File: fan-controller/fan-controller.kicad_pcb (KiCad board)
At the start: 2 copper layers, 80 x 60 mm, 23 parts, among them J1 DC_Jack_12V, J2 FAN1, J3 FAN2, J4 FAN3, J5 FAN4, U1 XIAO ESP32-C3, U2 AMS1117-5.0

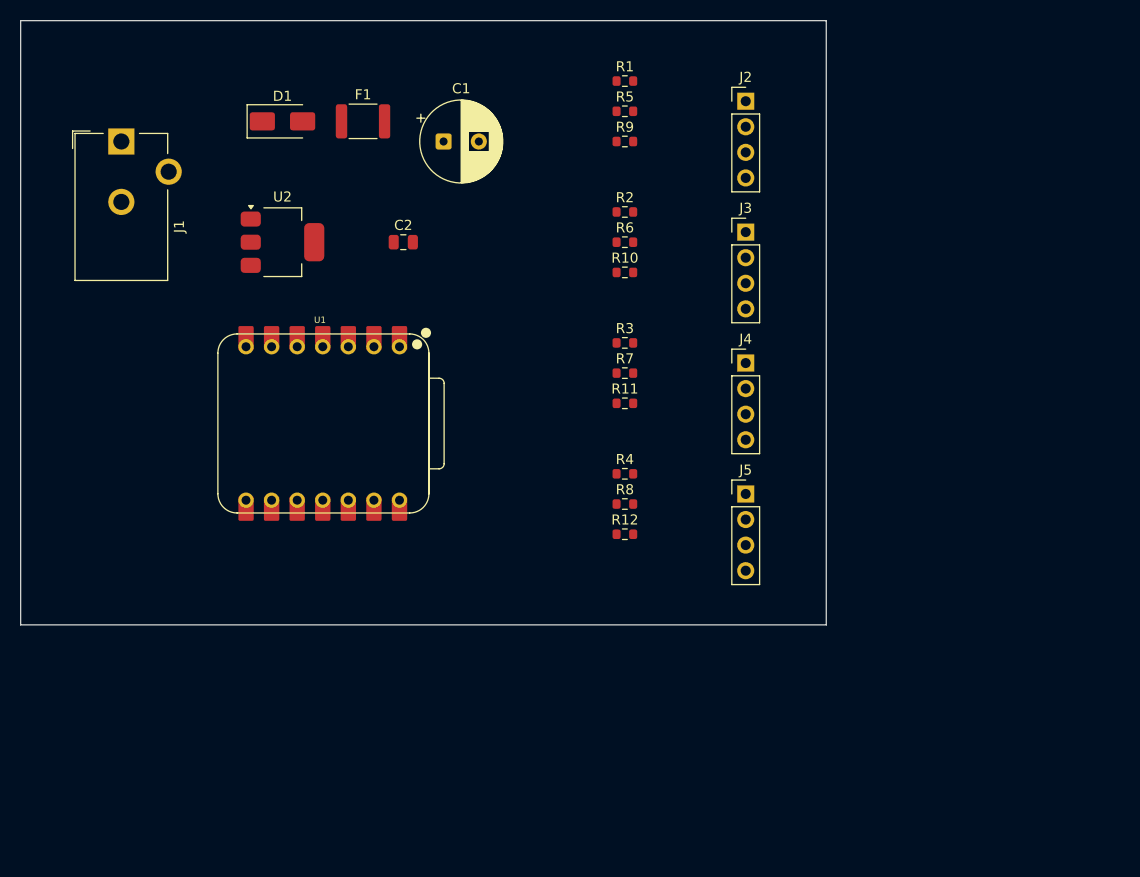
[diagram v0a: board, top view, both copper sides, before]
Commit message: Fold every schematic step into generate.py; swap fan pin pairs
generate.py is now the only command needed to rebuild the schematic. It runs
the full sequence, because each step used to be separate and every one of them
was forgotten at least once:

  1. reposition symbols and redraw all nets   (validated before writing)
  2. repair structural defects                (was fix_sch.py, now deleted)
  3. re-attach PWR_FLAGs and no-connects      (was an ad-hoc snippet, retyped
                                               by hand three times)
  4. verify the netlist against netplan.py    (was a separate audit)

Step 4 matters most: ERC cannot catch a wire landing on the wrong real pin,
since that is still a legal connection. Only a pin-by-pin netlist diff does.
--no-verify skips it where kicad-cli is unavailable.

Two latent bugs fixed while integrating:

  * Placed symbols were matched with a single-line regex, but KiCad rewrites
    the file with each field on its own line whenever the schematic is opened
    in the GUI. Regenerating after any GUI session found zero symbols and
    failed; fix_sch.py hit the same thing but failed silently, reporting
    success while repairing nothing. Both paths now use a whitespace-tolerant
    SYMBOL_RE, and a symbol's (at ...) is rewritten by matched span rather
    than by reconstructing the literal text.

  * netplan.py had lost pin_abs_rot, which only ever existed in a session
    scratchpad that a crash wiped. Restored and re-verified empirically
    against all four rotations before use.

Also swaps the XIAO pins between FAN1/FAN2 and FAN3/FAN4 as requested:
  FAN1 D1/D2 (2,3)   FAN2 D3/D4 (4,5)
  FAN3 D7/D10 (8,11) FAN4 D5/D6 (6,7)

PCB synced: 16 U1 pad assignments updated (8 pins x 2, since the DIP
footprint pairs an SMD and a through-hole pad per number). All 22 nets
cross-checked between schematic and board.

Board also reworked earlier in this session: outline fitted to the ground
zone at 76.5 x 29 mm (was 80 x 60), J1 m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
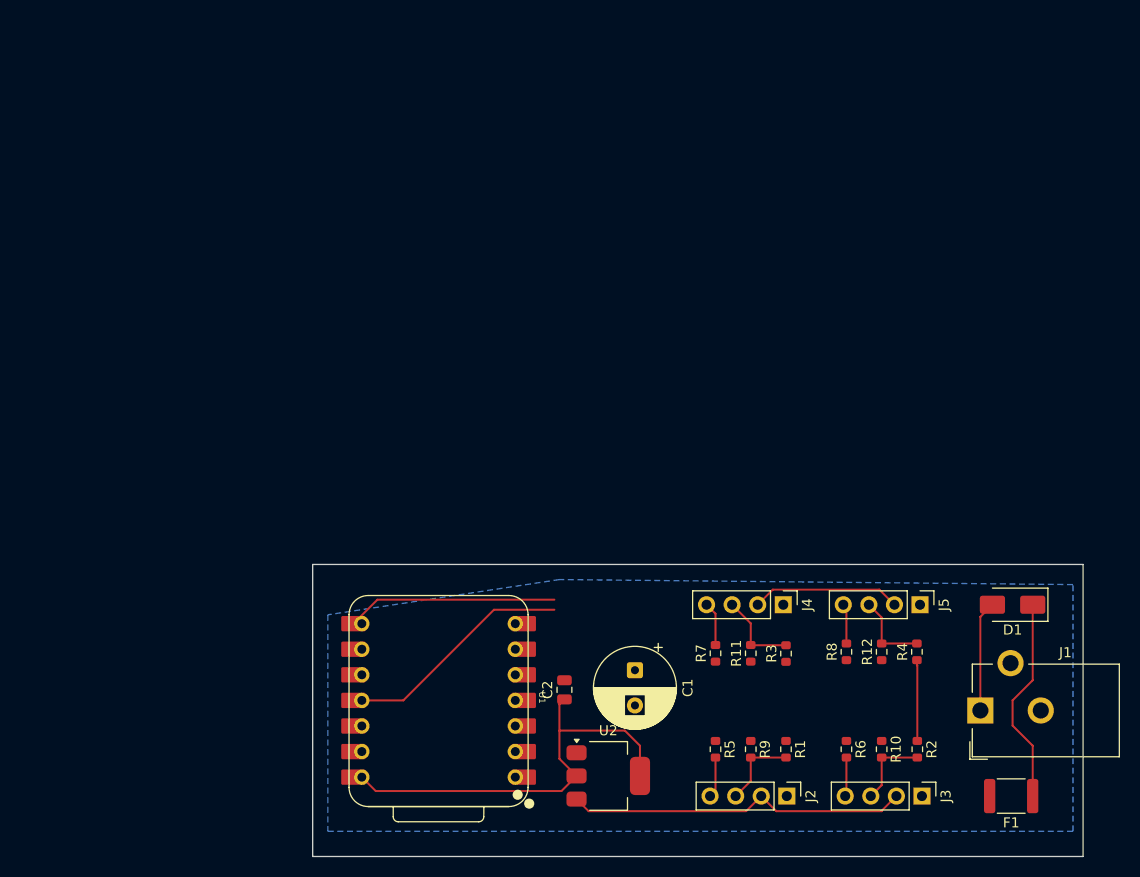
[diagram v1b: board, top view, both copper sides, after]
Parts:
- C1: footprint CP_Radial_D8.0mm_P3.50mm -> Capacitor_THT:CP_Radial_D8.0mm_P3.50mm
- C2: footprint C_0805_2012Metric -> Capacitor_SMD:C_0805_2012Metric
- D1: footprint D_SMA -> Diode_SMD:D_SMA
- F1: footprint Fuse_1812_4532Metric -> Fuse:Fuse_1812_4532Metric
- J1: footprint BarrelJack_CUI_PJ-102AH_Horizontal -> Connector_BarrelJack:BarrelJack_CUI_PJ-102AH_Horizontal
- J2, J3, J4, J5: footprint PinHeader_1x04_P2.54mm_Vertical -> Connector_PinHeader_2.54mm:PinHeader_1x04_P2.54mm_Vertical
- R1, R10, R11, R12, R2, R3, R4, R5, R6, R7, R8, R9: footprint R_0603_1608Metric -> Resistor_SMD:R_0603_1608Metric
- U1: footprint XIAO-ESP32-C3-DIP -> Seeed_Studio_XIAO_Series:XIAO-ESP32-C3-DIP
- U2: footprint SOT-223-3_TabPin2 -> Package_TO_SOT_SMD:SOT-223-3_TabPin2
- moved J1 102.3 mm to (95.3, 68.5), turned to 90 degrees
- moved F1 92.9 mm to (98.4, 77.0), turned to 180 degrees
- moved D1 86.9 mm to (98.5, 58.0), turned to 180 degrees
- moved J2 69.1 mm to (76.1, 77.0), turned to -90 degrees
- moved R1 68.3 mm to (76.0, 72.3), turned to -90 degrees
- moved R5 64.0 mm to (69.0, 72.3), turned to -90 degrees
- moved U2 62.1 mm to (58.4, 75.0)
- moved R9 61.6 mm to (72.5, 72.3), turned to -90 degrees
- moved R2 60.7 mm to (89.0, 72.3), turned to -90 degrees
- moved J3 58.7 mm to (89.5, 77.0), turned to -90 degrees
- moved C1 55.8 mm to (61.0, 64.5), turned to -90 degrees
- moved R6 54.9 mm to (82.0, 72.3), turned to -90 degrees
- moved R10 53.8 mm to (85.5, 72.3), turned to -90 degrees
- moved C2 47.2 mm to (54.0, 66.5), turned to 90 degrees
- moved R3 34.8 mm to (76.0, 62.9), turned to 90 degrees
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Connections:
- U1 pad 11: /FAN4_TACH -> /FAN3_TACH
- U1 pad 6: /FAN3_PWM -> /FAN4_PWM
- U1 pad 7: /FAN3_TACH -> /FAN4_TACH
- U1 pad 8: /FAN4_PWM -> /FAN3_PWM
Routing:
- net /+12V_PROT: track 0.00 -> 49.0 mm
- net /+5V: track 0.00 -> 42.6 mm
- net /FAN3_TACH: track 0.00 -> 22.8 mm
- net /FAN3_PWM: track 0.00 -> 20.9 mm
- net /+12V_FUSED: track 0.00 -> 20.7 mm
- net /+12V_IN: track 0.00 -> 11.0 mm
- net /FAN3_TACH_RAW: track 0.00 -> 8.28 mm
- net /+3V3: track 0.00 -> 8.04 mm
- net /FAN1_TACH_RAW: track 0.00 -> 7.95 mm
- net /FAN4_TACH_RAW: track 0.00 -> 7.88 mm
- net /FAN2_TACH_RAW: track 0.00 -> 7.81 mm
- net /FAN3_PWM_OUT: track 0.00 -> 4.37 mm
- net /FAN1_PWM_OUT: track 0.00 -> 4.05 mm
- net /FAN4_PWM_OUT: track 0.00 -> 3.98 mm
- net /FAN2_PWM_OUT: track 0.00 -> 3.87 mm
- added copper zone on B.Cu, net /GND
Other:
- board size 80 x 60 mm -> 76.5 x 29 mm

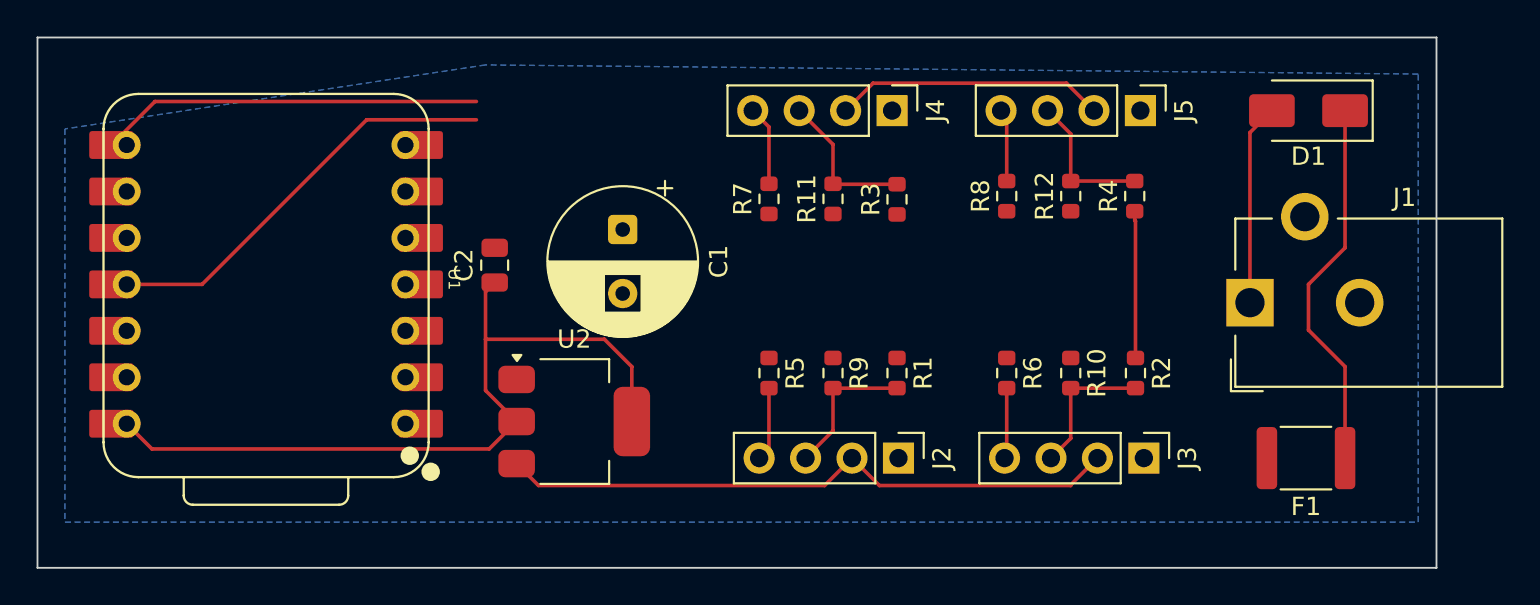
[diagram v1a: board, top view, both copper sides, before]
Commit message: Route the board: ground plane, wider power nets, jack on the edge
The PCB is now fully routed. 167 tracks, 7 vias, no unconnected pads.

Layout
  Board shrunk from 80 x 60 mm to 72.9 x 25.0 mm, fitted 1mm clear of all
  copper. J1 sits on the right end opposite the XIAO with its flange on the
  board edge, so the 3.5mm barrel protrudes as a panel-mount jack should.
  Getting there took two goes: the flange initially sat 1.9mm inboard of the
  edge, making the plug look adrift. Moving the plug pocket (J1, F1, D1 plus
  9 tracks) 1.8mm inward fixed it. 3mm was requested but drives F1's pad and
  the +12V_IN wire into the +12V_PROT trunk at x=91.5; 1.8mm is the limit
  before that clash. Only the 2 tracks crossing the pocket boundary needed
  shortening, exactly as predicted.

Ground plane
  GND pour on B.Cu, 1417mm^2, thermal relief on pads. A keep-out clears the
  copper away from the XIAO's antenna: U1 is rotated -90 so pins 7 and 8 both
  sit at y=59.88, the module's top edge, which is the antenna end opposite
  the USB connector. The window stops at y=58.6, clearing those two pads by
  0.52mm - an earlier attempt ran to y=60.0 and DRC rightly rejected it for
  swallowing them.

Track widths
  Power and ground widened from the 0.2mm minimum (0.74A) to targets from
  IPC-2152 at 1oz, 10C rise. A single width does not fit: the corridor around
  U1 is a 2.54mm pad pitch. So each segment starts at target and steps down
  only where DRC objects.

    +12V_IN, +12V_FUSED, +12V_PROT   1.0mm    2.39 A
    GND                              1.0mm    2.39 A  (2 segments 0.2mm)
    +5V, +3V3                        0.6mm    1.65 A

  The 12V rail feeds four fans through a 1.5A-hold polyfuse, so 2.39A leaves
  real margin. The two 0.2mm GND segments run directly over the B.Cu plane -
  sampling along their length found plane copper at 28 of 33 points, and U1's
  GND pad is a through-hole tied into it - so the plane carries that return
  in parallel and width is not the limit ther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
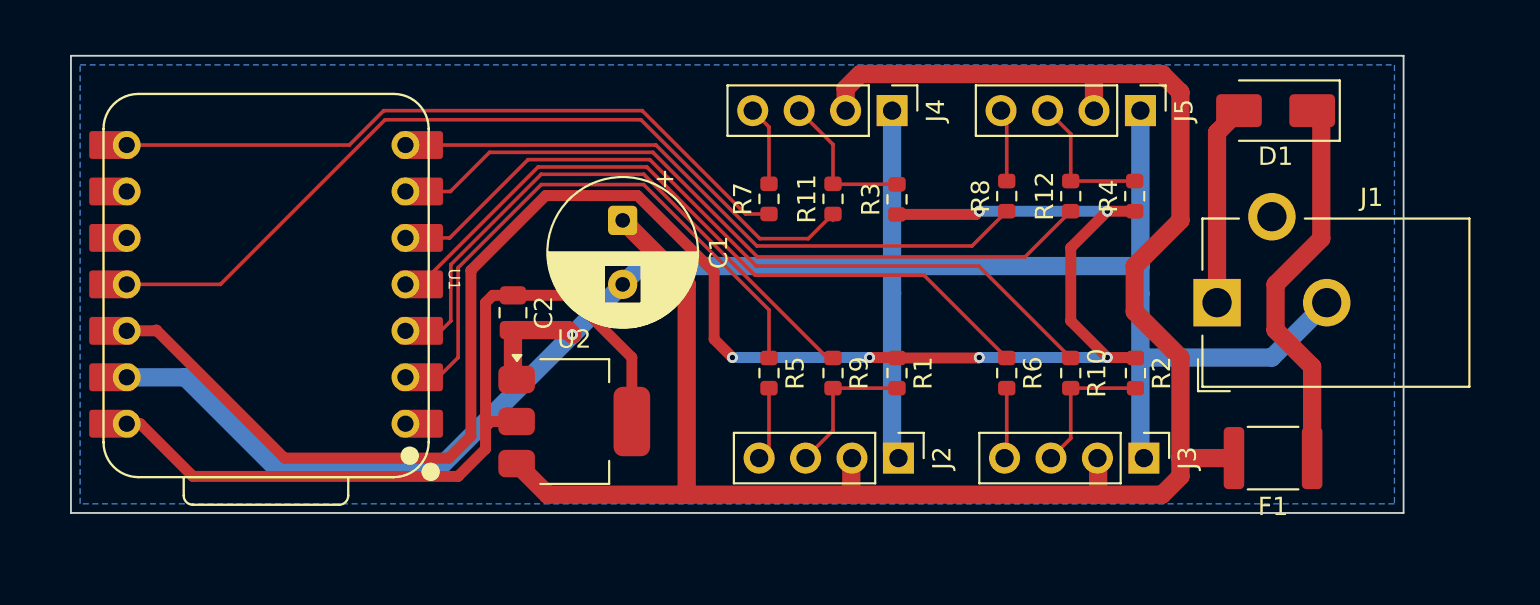
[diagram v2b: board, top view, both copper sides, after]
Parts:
- moved C2 2.79 mm to (55.0, 69.0), turned to -90 degrees
- moved D1 1.80 mm to (96.7, 58.0)
- moved F1 1.80 mm to (96.6, 77.0)
- moved J1 1.80 mm to (93.5, 68.5)
- moved C1 0.50 mm to (61.0, 64.0)
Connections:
- U1 pad 6: /FAN4_PWM -> /FAN4_TACH
- U1 pad 7: /FAN4_TACH -> /FAN4_PWM
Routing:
- net /GND: track 0.00 -> 117.8 mm, vias 0 -> 1
- net /+3V3: track 8.04 -> 97.9 mm, vias 0 -> 6
- net /+12V_PROT: track 49.0 -> 106.2 mm
- net /FAN2_TACH: track 0.00 -> 41.8 mm
- net /FAN2_PWM: track 0.00 -> 40.3 mm
- net /FAN4_TACH: track 0.00 -> 39.8 mm
- net /FAN4_PWM: track 0.00 -> 35.1 mm
- net /FAN1_TACH: track 0.00 -> 32.1 mm
- net /FAN1_PWM: track 0.00 -> 31.9 mm
- net /FAN3_TACH: track 22.8 -> 45.9 mm
- net /FAN3_PWM: track 20.9 -> 38.2 mm
- net /+5V: track 42.6 -> 44.2 mm
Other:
- board size 76.5 x 29 mm -> 72.9 x 25 mm

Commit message: Add back-side silkscreen: project name, author, year
Zwei Zeilen auf B.SilkS, mittig zwischen den Steckern bei (74.8, 66.5/69.0):

    Fan Controller v1
    Joachim Banzhaf 2026

1mm Texthoehe, gespiegelt (SetMirrored) - sonst stuende die Beschriftung
beim Blick auf die Unterseite seitenverkehrt. Die Rueckseite war bis jetzt
voellig leer; die einzige freie Flaeche ist 24x4mm, daher die kompakte
Groesse.

Der Text ueberdeckt kein Pad und keine Durchkontaktierung. DRC unveraendert:
die 14 silk_over_copper- und 3 silk_edge_clearance-Meldungen stammen
saemtlich von vorhandenen Bauteil-Bezeichnern auf der Oberseite, keine
betrifft den neuen Text.

Fertigungspaket neu erzeugt: B_Silkscreen.gbo waechst von 460 B auf 15.8 KB
(638 Zeichenoperationen), Zip auf 46.5 KB.

Rueckseiten-Siebdruck kostet bei allen drei Kandidaten nichts extra.
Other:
- board text added: "Fan Controller v1"
- board text added: "Joachim Banzhaf 2026"
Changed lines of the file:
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@@
 		(layer "Edge.Cuts")
+	)
+	(gr_text "Fan Controller v1"
+		(at 74.8 66.5 0)
+		(layer "B.SilkS")
+		(effects
+			(font
+				(size 1 1)
+				(thickness 0.15)
+			)
+			(justify mirror)
+		)
+	)
+	(gr_text "Joachim Banzhaf 2026"
+		(at 74.8 69 0)
+		(layer "B.SilkS")
+		(effects
+			(font
+				(size 1 1)
+				(thickness 0.15)
+			)
+			(justify mirror)
+		)
 	)
 	(segment
